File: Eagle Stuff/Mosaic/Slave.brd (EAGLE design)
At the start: 45.7 x 48.4 mm, 6 parts

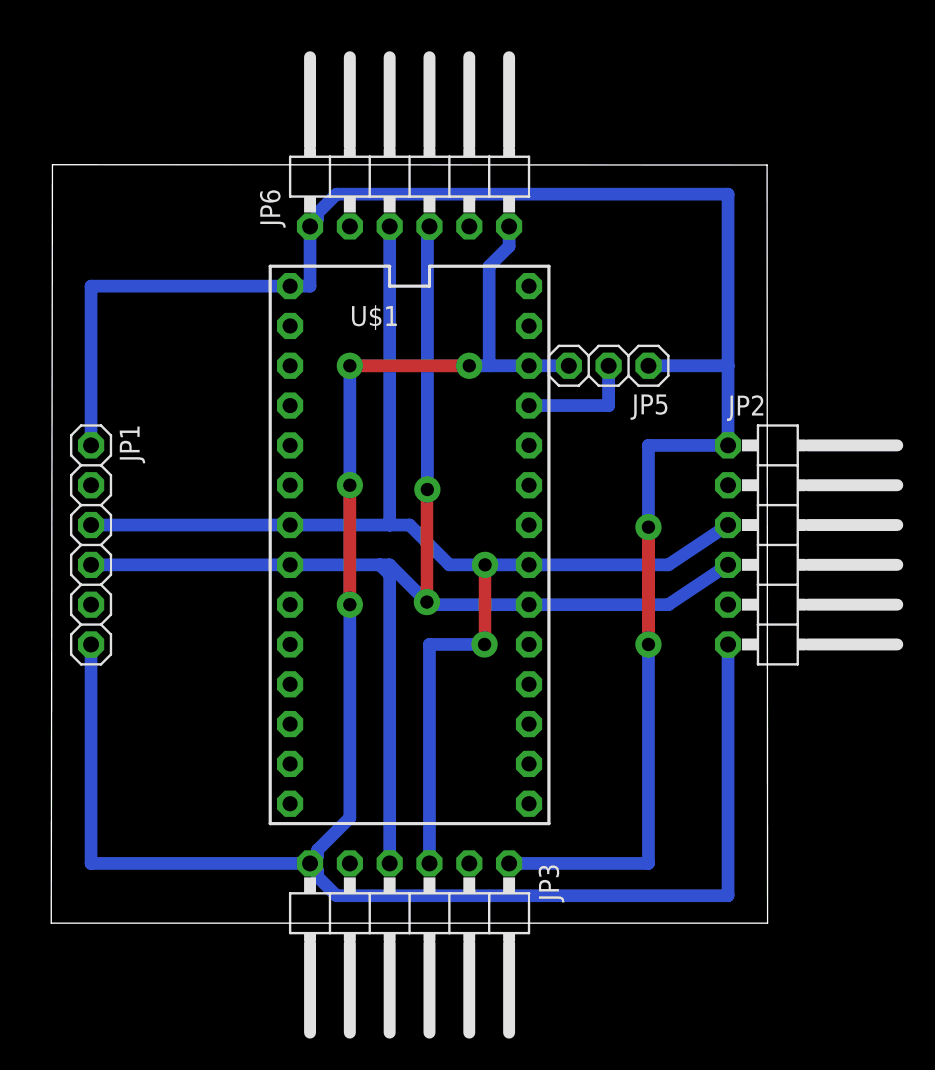
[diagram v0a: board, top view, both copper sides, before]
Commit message: Added I2C Connector, moved Slave board to origin
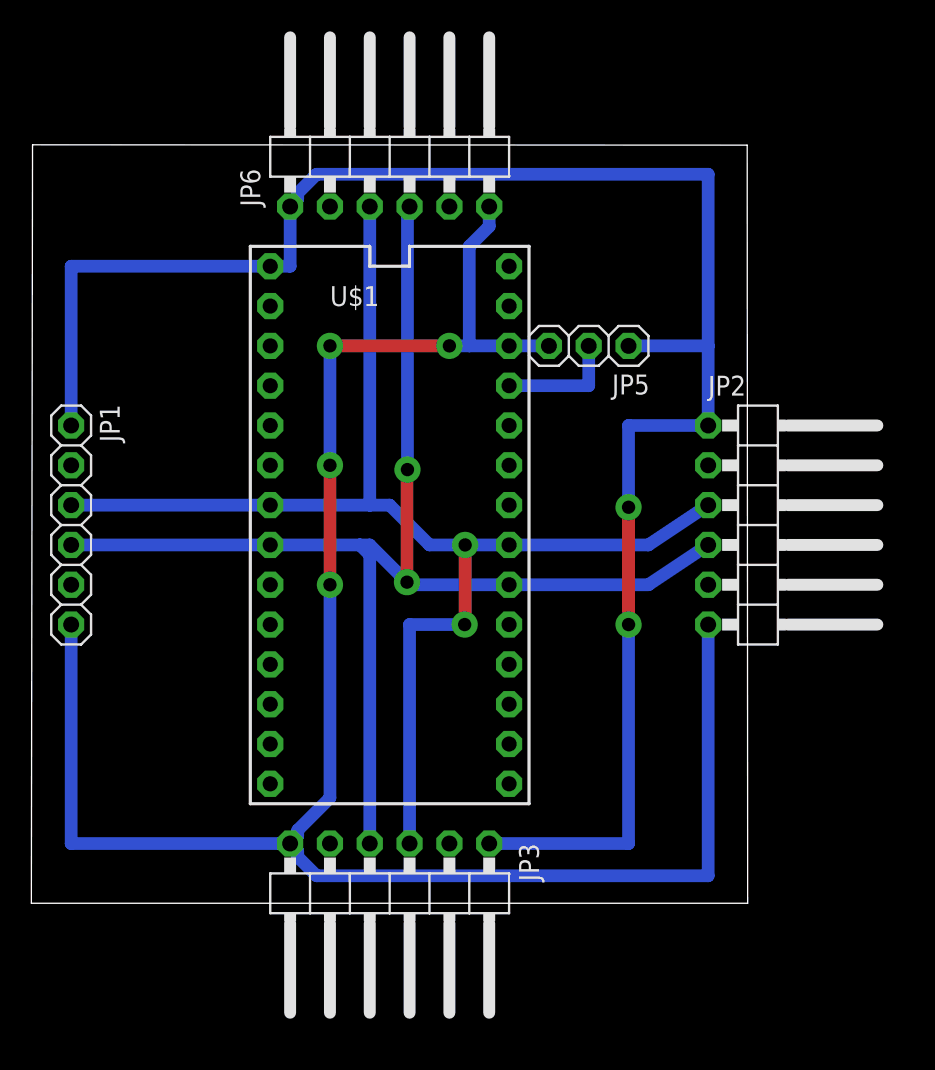
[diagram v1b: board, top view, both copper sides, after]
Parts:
- moved JP1 1.80 mm to (2.54, 24.1)
- moved JP3 1.80 mm to (22.9, 0.00)
- moved JP5 1.80 mm to (35.6, 35.6)
- moved U$1 1.80 mm to (22.9, 24.1)
- moved JP2 1.80 mm to (47.0, 24.1)
- moved JP6 1.80 mm to (22.9, 48.3)
